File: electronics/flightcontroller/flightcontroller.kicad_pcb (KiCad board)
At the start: 2 copper layers, 32 parts, among them J1 BATT, J2 ESC+, J3 ESC, J4 Servo3, J5 Servo2, J6 Servo1, J7 ESC-, SW1 SW_Push, U1 DS2745U, U2 MPU-9250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

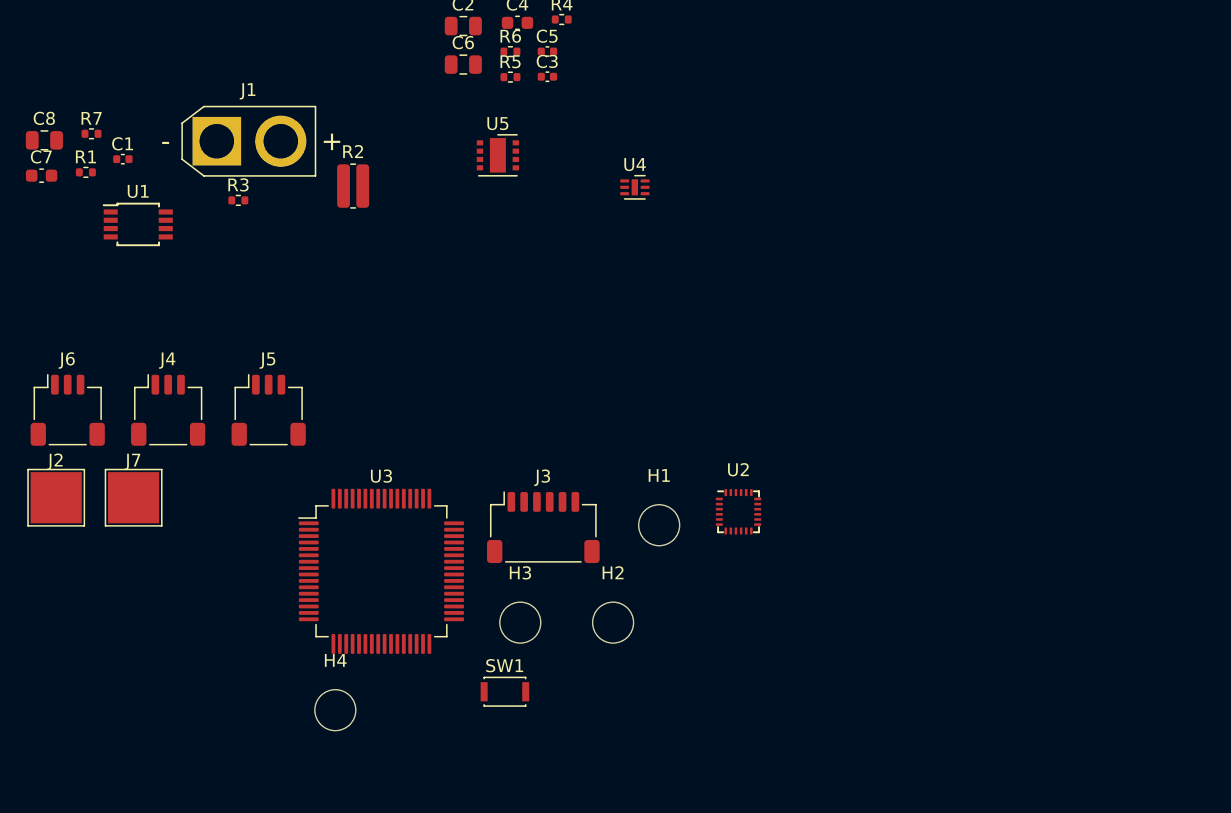
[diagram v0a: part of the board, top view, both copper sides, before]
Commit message: electronics: Draft most of the flight controller schematics.
The power supply part is not complete, and all connections to the MCU are
missing.
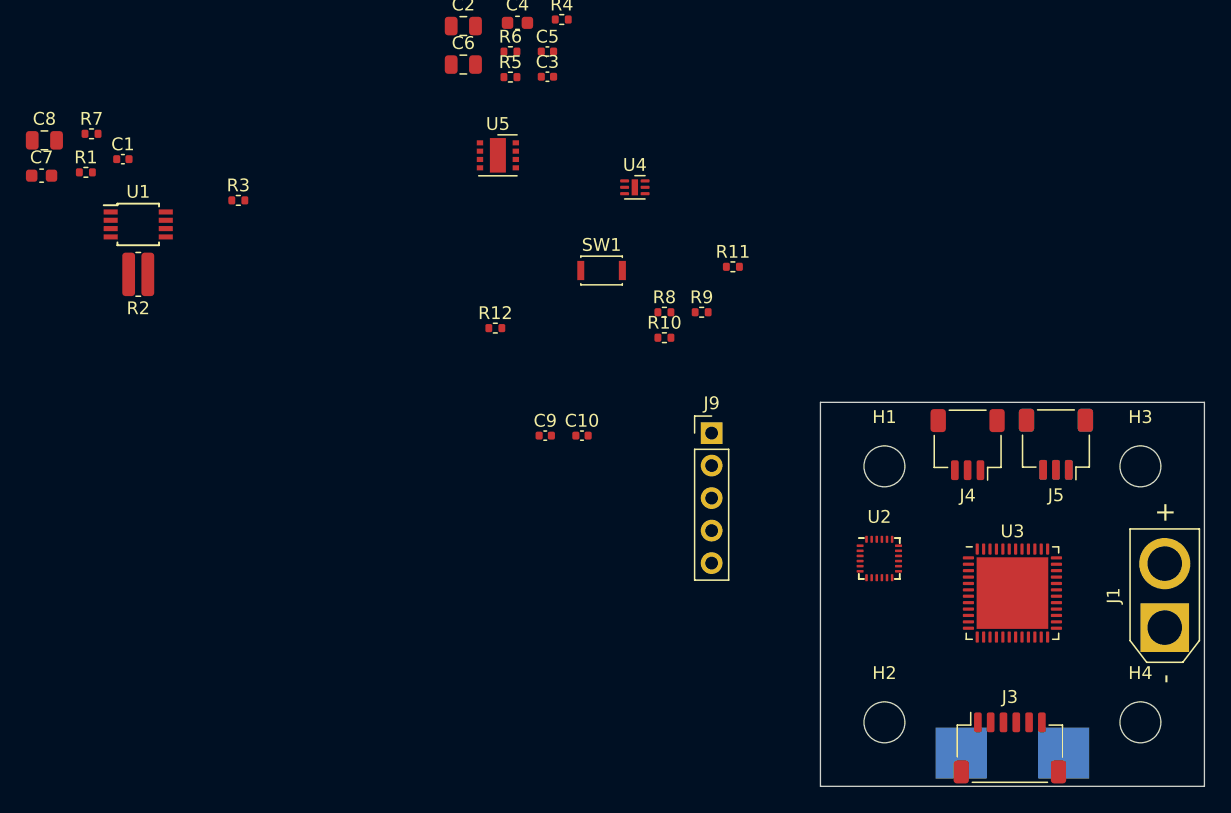
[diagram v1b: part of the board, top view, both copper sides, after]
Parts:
- added C10: 0.1uF, Capacitor_SMD:C_0402_1005Metric, F.Cu at (166.4, 67.6)
- added C9: 0.1uF, Capacitor_SMD:C_0402_1005Metric, F.Cu at (163.5, 67.6)
- added J9: SWD, Connector_PinHeader_2.54mm:PinHeader_1x05_P2.54mm_Vertical, F.Cu at (176.5, 67.4)
- added R10: 47k, Resistor_SMD:R_0402_1005Metric, F.Cu at (172.8, 60.0)
- added R11: 47k, Resistor_SMD:R_0402_1005Metric, F.Cu at (178.2, 54.4)
- added R12: 10k, Resistor_SMD:R_0402_1005Metric, F.Cu at (159.6, 59.2)
- added R8: 47k, Resistor_SMD:R_0402_1005Metric, F.Cu at (172.8, 58.0)
- added R9: 47k, Resistor_SMD:R_0402_1005Metric, F.Cu at (175.7, 58.0)
- J2, J6, J7: moved to B.Cu
- U3: value STM32F373RBTx -> STM32L462CEUx; footprint Package_QFP:LQFP-64_10x10mm_P0.5mm -> Package_DFN_QFN:QFN-48-1EP_7x7mm_P0.5mm_EP5.6x5.6mm
- moved J1 83.2 mm to (211.9, 82.6), turned to 90 degrees
- moved J2 81.2 mm to (204.0, 92.4), turned to 180 degrees
- moved J6 77.3 mm to (203.4, 68.3)
- moved J7 67.7 mm to (196.0, 92.4), turned to 180 degrees
- moved H4 62.9 mm to (210.0, 90.0)
- moved J4 62.5 mm to (196.5, 68.3), turned to 180 degrees
- moved J5 61.6 mm to (203.4, 68.3), turned to 180 degrees
- moved H3 50.0 mm to (210.0, 70.0)
- moved U3 49.3 mm to (200.0, 79.9)
- moved J3 40.3 mm to (199.8, 92.0)
- moved SW1 33.8 mm to (167.9, 54.7)
- moved H2 22.6 mm to (190.0, 90.0)
- moved H1 18.2 mm to (190.0, 70.0)
- moved R2 18.2 mm to (131.7, 55.0), turned to 180 degrees
- moved U2 11.6 mm to (189.6, 77.2)
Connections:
- SW1 pad 1: unconnected-(SW1-Pad1) -> /MCU/~{RESET}
- SW1 pad 2: unconnected-(SW1-Pad2) -> GND
- U2 pad 1: unconnected-(U2-Pad1) -> Net-(U2-Pad1)
- U2 pad 10: unconnected-(U2-Pad10) -> Net-(U2-Pad10)
- U2 pad 18: unconnected-(U2-Pad18) -> GND
- U2 pad 20: unconnected-(U2-Pad20) -> GND
- U3 pad 1: unconnected-(U3-Pad1) -> +3V3
- U3 pad 23: unconnected-(U3-Pad23) -> GND
- U3 pad 24: unconnected-(U3-Pad24) -> +3V3
- U3 pad 35: unconnected-(U3-Pad35) -> GND
- U3 pad 36: unconnected-(U3-Pad36) -> +3V3
- U3 pad 47: unconnected-(U3-Pad47) -> GND
- U3 pad 48: unconnected-(U3-Pad48) -> +3V3
- U3 pad 49: unconnected-(U3-Pad49) -> GND
- U3 pad 7: unconnected-(U3-Pad7) -> /MCU/~{RESET}
- U3 pad 8: unconnected-(U3-Pad8) -> GND
- U3 pad 9: unconnected-(U3-Pad9) -> +3V3
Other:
- board outline added: 30 x 30 mm

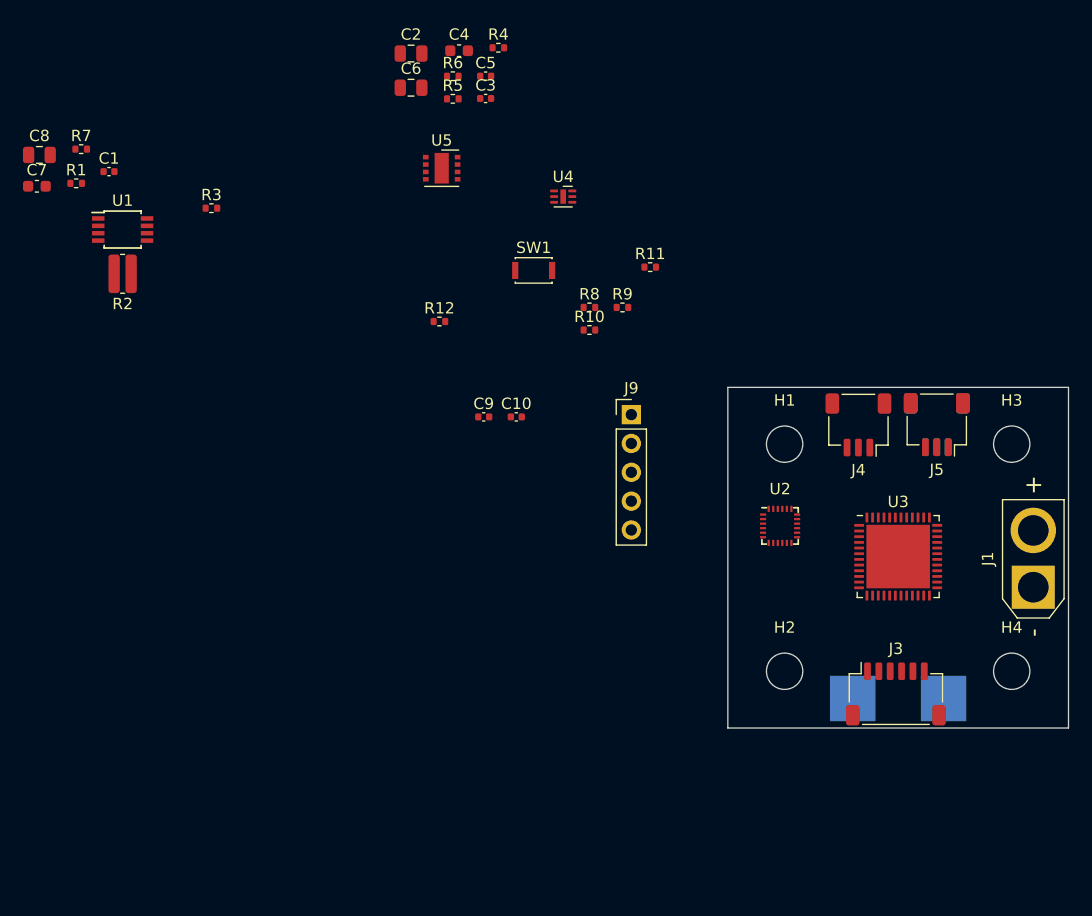
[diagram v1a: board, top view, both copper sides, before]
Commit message: PCB: USB, micro SD, and many component changes.
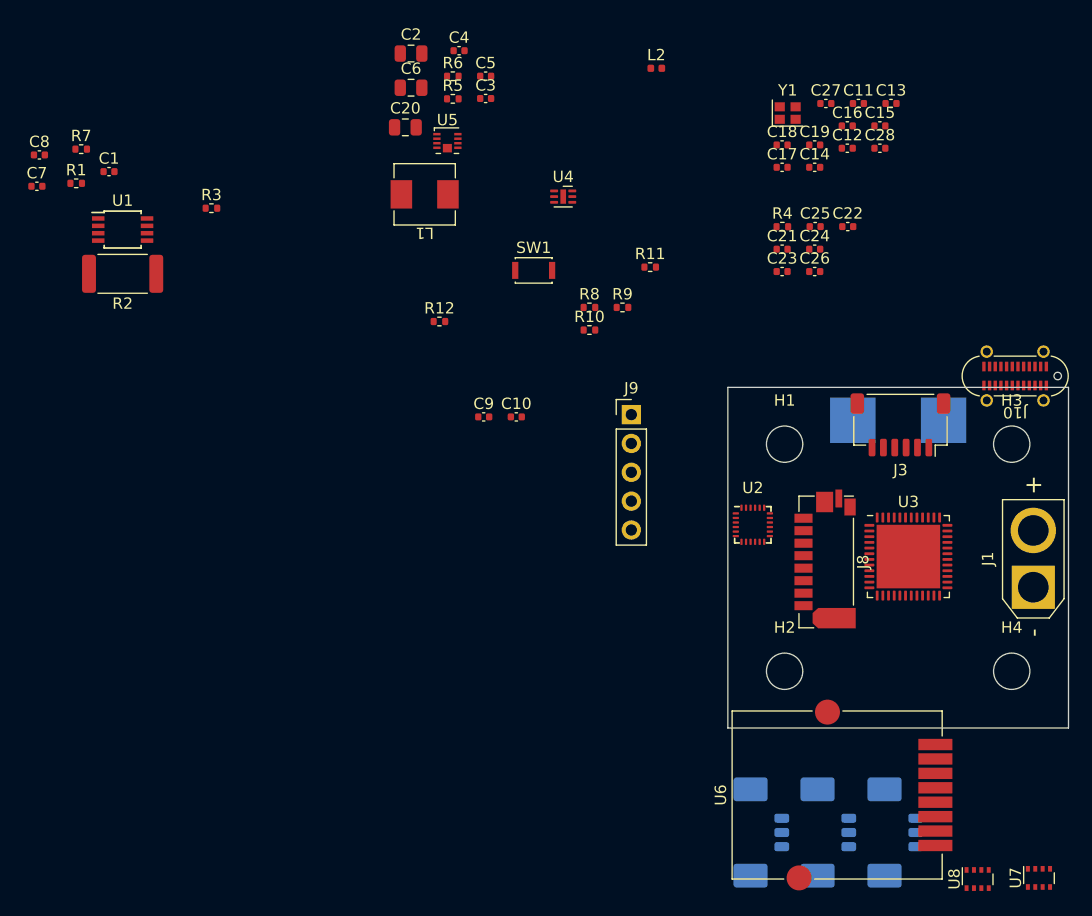
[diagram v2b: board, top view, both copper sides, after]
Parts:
- added C11: 10uF/6.3V, Capacitor_SMD:C_0402_1005Metric, F.Cu at (196.5, 40.0)
- added C12: 0.1uF, Capacitor_SMD:C_0402_1005Metric, F.Cu at (195.5, 43.9)
- added C13: 0.1uF, Capacitor_SMD:C_0402_1005Metric, F.Cu at (199.4, 40.0)
- added C14: 0.1uF, Capacitor_SMD:C_0402_1005Metric, F.Cu at (192.7, 45.6)
- added C15: 0.1uF, Capacitor_SMD:C_0402_1005Metric, F.Cu at (198.4, 42.0)
- added C16: 0.1uF, Capacitor_SMD:C_0402_1005Metric, F.Cu at (195.5, 42.0)
- added C17: 0.1uF, Capacitor_SMD:C_0402_1005Metric, F.Cu at (189.8, 45.6)
- added C18: 10uF/6.3V, Capacitor_SMD:C_0402_1005Metric, F.Cu at (189.8, 43.6)
- added C19: 10uF/6.3V, Capacitor_SMD:C_0402_1005Metric, F.Cu at (192.7, 43.6)
- added C20: 22uF/6.3V, Capacitor_SMD:C_0805_2012Metric, F.Cu at (156.6, 42.1)
- added C21: 0.1uF, Capacitor_SMD:C_0402_1005Metric, F.Cu at (189.8, 52.8)
- added C22: 0.1uF, Capacitor_SMD:C_0402_1005Metric, F.Cu at (195.6, 50.8)
- added C23: 10uF/6.3V, Capacitor_SMD:C_0402_1005Metric, F.Cu at (189.8, 54.8)
- added C24: 10uF/6.3V, Capacitor_SMD:C_0402_1005Metric, F.Cu at (192.7, 52.8)
- added C25: 10uF/6.3V, Capacitor_SMD:C_0402_1005Metric, F.Cu at (192.7, 50.8)
- added C26: 10uF/6.3V, Capacitor_SMD:C_0402_1005Metric, F.Cu at (192.7, 54.8)
- added C27: 6.8pF, Capacitor_SMD:C_0402_1005Metric, F.Cu at (193.6, 40.0)
- added C28: 6.8pF, Capacitor_SMD:C_0402_1005Metric, F.Cu at (198.4, 43.9)
- added J10: USB, flightcontroller-footprints:USB_C_Receptacle_Amphenol_12402032, F.Cu at (210.3, 64.0)
- added J8: Micro_SD_Card_Det_HYC80-TF08-XXX, flightcontroller-footprints:HYC80-TF08-XXX, F.Cu at (193.2, 80.4)
- added L1: 3.3uH, flightcontroller-footprints:L_AVX_LMLP0506D, F.Cu at (158.3, 48.0)
- added L2: 600R@100MHz, Inductor_SMD:L_0402_1005Metric, F.Cu at (178.7, 36.9)
- added U6: GT-24-Mini, flightcontroller-footprints:GT-24-Mini, F.Cu at (194.6, 100.9)
- added U7: Omron_2SMPB-02B, flightcontroller-footprints:Omron_2SMPB, F.Cu at (212.4, 108.2)
- added U8: Omron_2SMPB-02B, flightcontroller-footprints:Omron_2SMPB, F.Cu at (207.0, 108.3)
- added Y1: 24MHz, Crystal:Crystal_SMD_2016-4Pin_2.0x1.6mm, F.Cu at (190.3, 40.8)
- C2: value 10uF -> 10uF/25V
- C3: value ? -> 3300pF
- C4: value 1uF/25V -> 1uF/10V; footprint Capacitor_SMD:C_0603_1608Metric -> Capacitor_SMD:C_0402_1005Metric
- C6: value 10uF -> 22uF/6.3V
- C7: value 1uF/25V -> 1uF/25V; footprint Capacitor_SMD:C_0603_1608Metric -> Capacitor_SMD:C_0402_1005Metric
- C8: value 10uF -> 10uF/6.3V; footprint Capacitor_SMD:C_0805_2012Metric -> Capacitor_SMD:C_0402_1005Metric
- J4, J5: footprint Connector_JST:JST_SH_SM03B-SRSS-TB_1x03-1MP_P1.00mm_Horizontal -> Connector_Molex:Molex_PicoBlade_53398-0371_1x03-1MP_P1.25mm_Vertical; moved to B.Cu
- J6: footprint Connector_JST:JST_SH_SM03B-SRSS-TB_1x03-1MP_P1.00mm_Horizontal -> Connector_Molex:Molex_PicoBlade_53398-0371_1x03-1MP_P1.25mm_Vertical
- R2: footprint Resistor_SMD:R_0612_1632Metric -> Resistor_SMD:R_2512_6332Metric
- R4: value ? -> 330
- R5: value 18k -> 68k
- R6: value 3k -> 16k
- SW1: value SW_Push -> RESET
- U5: value AOZ6663DI -> BD9D322QWZ; footprint flightcontroller-footprints:DFN-6-1EP_3x3mm_P0.65mm_EP1.25x2.7mm -> flightcontroller-footprints:Rohm_BD9D322QWZ
- moved J5 38.9 mm to (188.5, 104.2), turned to 90 degrees
- moved J6 37.0 mm to (194.4, 104.2), turned to 90 degrees
- moved J4 36.1 mm to (200.3, 104.2), turned to 90 degrees
- moved R4 29.6 mm to (189.8, 50.9)
- moved J2 25.8 mm to (196.0, 67.9), turned to 0 degrees
- moved J7 25.8 mm to (204.0, 67.9), turned to 0 degrees
- moved J3 23.7 mm to (200.2, 68.3), turned to 180 degrees
- moved U5 2.45 mm to (160.3, 43.3)
- moved U2 2.40 mm to (187.2, 77.1)
- moved U3 0.90 mm to (200.9, 79.9)
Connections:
- R4 pad 1: Net-(R4-Pad1) -> /Sensors/PR_MISO
- R4 pad 2: Net-(C3-Pad1) -> Net-(R4-Pad2)
- U2 pad 11: unconnected-(U2-Pad11) -> /Sensors/IMU_FSYNC
- U2 pad 12: unconnected-(U2-Pad12) -> /Sensors/IMU_INT
- U2 pad 13: unconnected-(U2-Pad13) -> +3V3
- U2 pad 22: unconnected-(U2-Pad22) -> /Sensors/IMU_~{CS}
- U2 pad 23: unconnected-(U2-Pad23) -> /Sensors/IMU_SCLK
- U2 pad 24: unconnected-(U2-Pad24) -> /Sensors/IMU_MOSI
- U2 pad 8: unconnected-(U2-Pad8) -> +3V3
- U2 pad 9: unconnected-(U2-Pad9) -> /Sensors/IMU_MISO
- U5 pad 1: GND -> +BATT
- U5 pad 2: Net-(C5-Pad2) -> Net-(C5-Pad1)
- U5 pad 3: +BATT -> Net-(C5-Pad2)
- U5 pad 4: Net-(R4-Pad1) -> GND
- U5 pad 5: Net-(C4-Pad1) -> Net-(C3-Pad1)
- U5 pad 7: +BATT -> Net-(C4-Pad1)
- U5 pad 8: Net-(C5-Pad1) -> +BATT

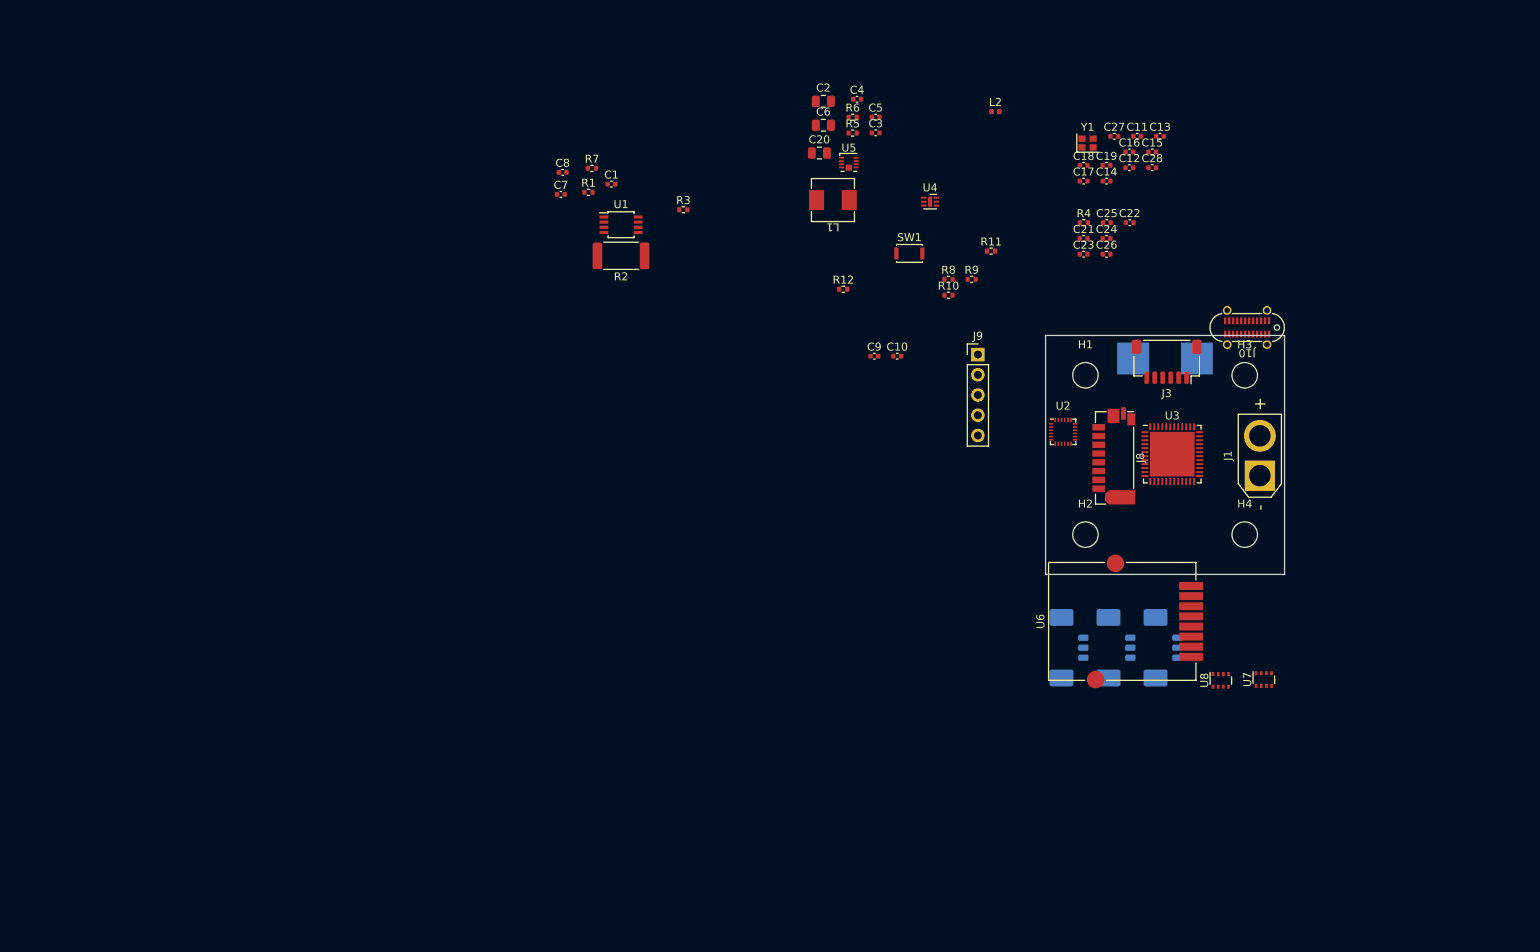
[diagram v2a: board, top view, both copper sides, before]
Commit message: electronics: General PCB layout and size, let pressure sensors use I2C.
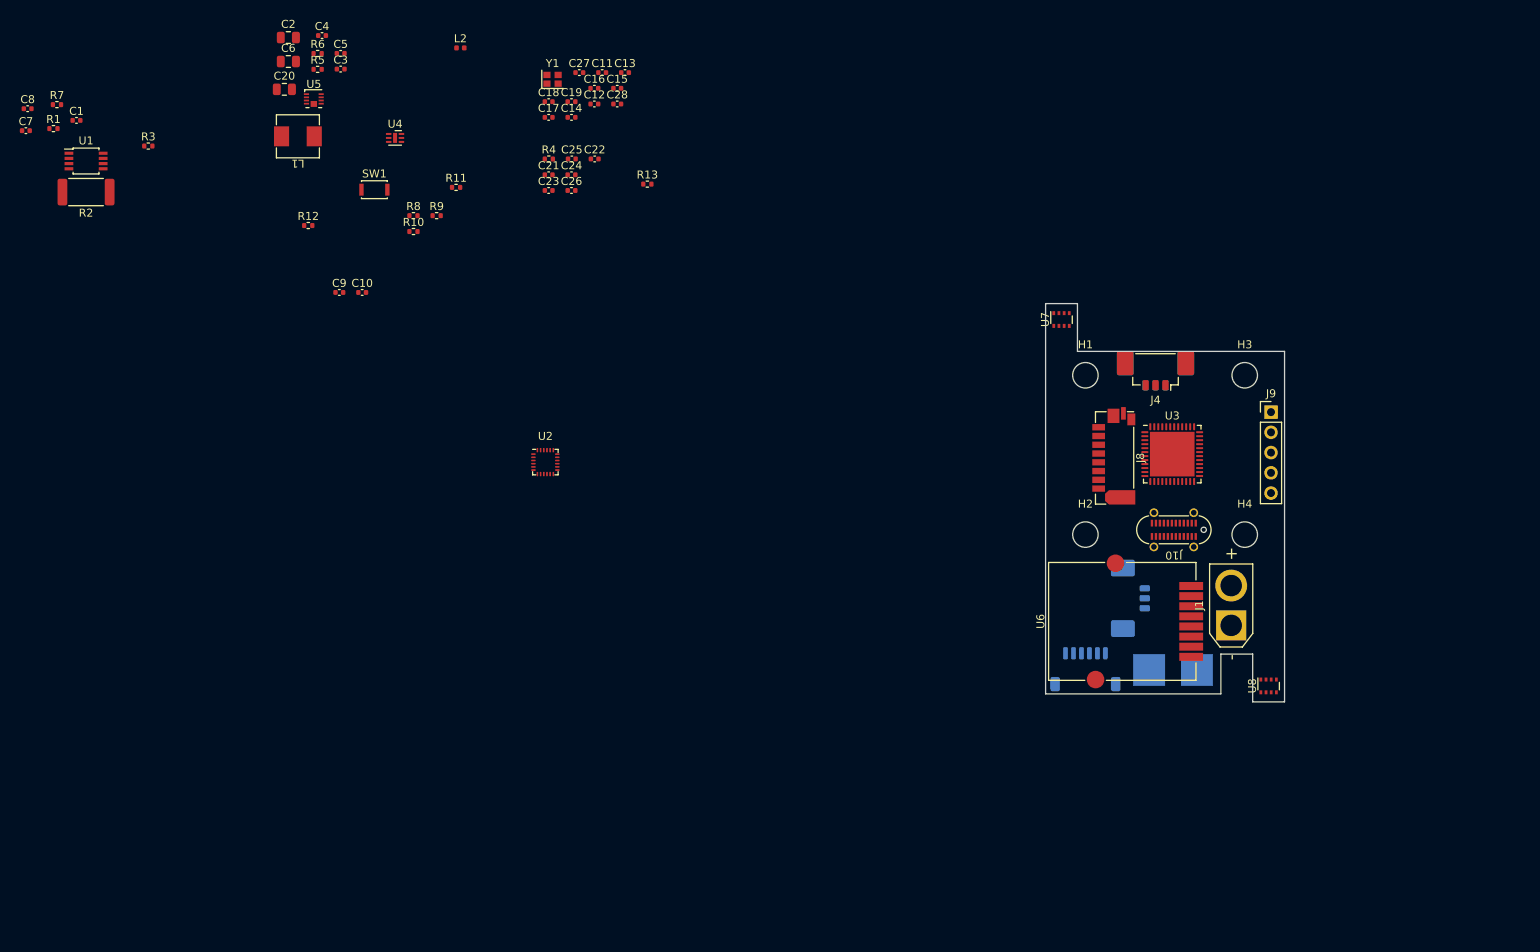
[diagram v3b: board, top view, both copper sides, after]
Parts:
- added R13: 10k, Resistor_SMD:R_0402_1005Metric, F.Cu at (135.0, 46.0)
- J3: moved to B.Cu
- J4: moved to F.Cu
- R4: value 330 -> 10k
- moved C12 67.6 mm to (128.3, 35.9)
- moved C13 67.6 mm to (132.2, 32.0)
- moved C16 67.6 mm to (128.3, 34.0)
- moved C22 67.6 mm to (128.4, 42.8)
- moved C4 67.6 mm to (94.2, 27.4)
- moved C7 67.6 mm to (57.0, 39.3)
- moved L1 67.6 mm to (91.1, 40.0)
- moved R3 67.6 mm to (72.3, 41.2)
- moved R4 67.6 mm to (122.6, 42.9)
- moved R7 67.6 mm to (60.9, 36.0)
- moved U5 67.6 mm to (93.1, 35.3)
- moved Y1 67.6 mm to (123.1, 32.8)
- moved C1 67.6 mm to (63.3, 38.0)
- moved C10 67.6 mm to (99.2, 59.6)
- moved C14 67.6 mm to (125.5, 37.6)
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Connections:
- net /Sensors/PR_MISO renamed Net-(R4-Pad1)
- net /Sensors/PR_MOSI renamed /Sensors/PR_SDA
- net /Sensors/PR_SCK renamed /Sensors/PR_SCL
- net Net-(U7-Pad1) renamed /Sensors/PR_RST
- R4 pad 2: Net-(R4-Pad2) -> GND
- U7 pad 2: /Sensors/PR1_~{CS} -> +3V3
- U8 pad 2: /Sensors/PR1_~{CS} -> +3V3
- U8 pad 5: Net-(R4-Pad2) -> Net-(U8-Pad5)
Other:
- board size 30 x 30 mm -> 30 x 50 mm
- board text added: "Direction of flight"
